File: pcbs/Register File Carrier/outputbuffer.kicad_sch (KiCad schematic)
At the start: 2 parts, among them U4001 74HC245, U4002 74HC245

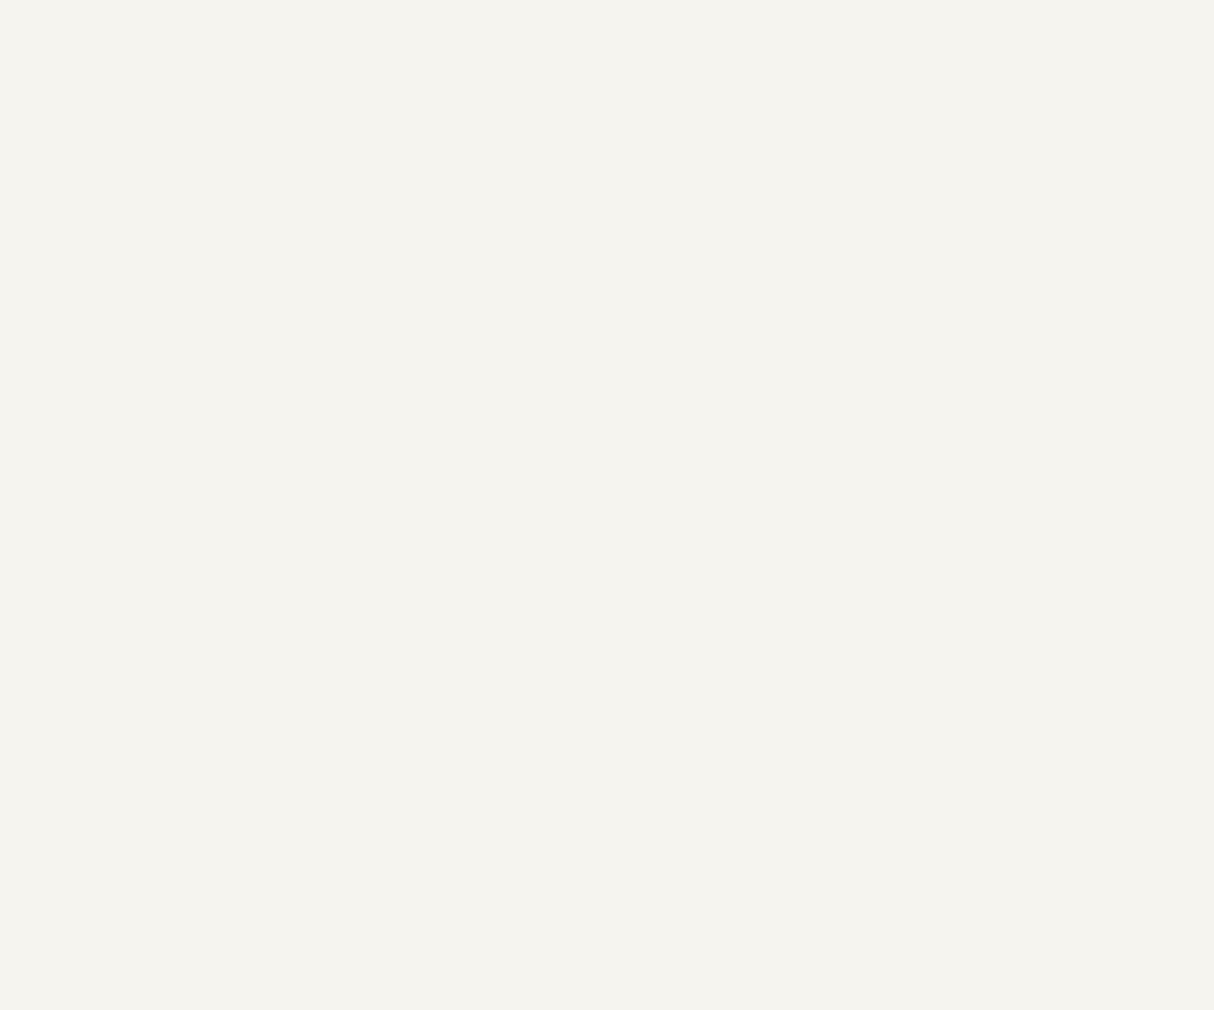
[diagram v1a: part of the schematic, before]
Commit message: Setting up some LEDs
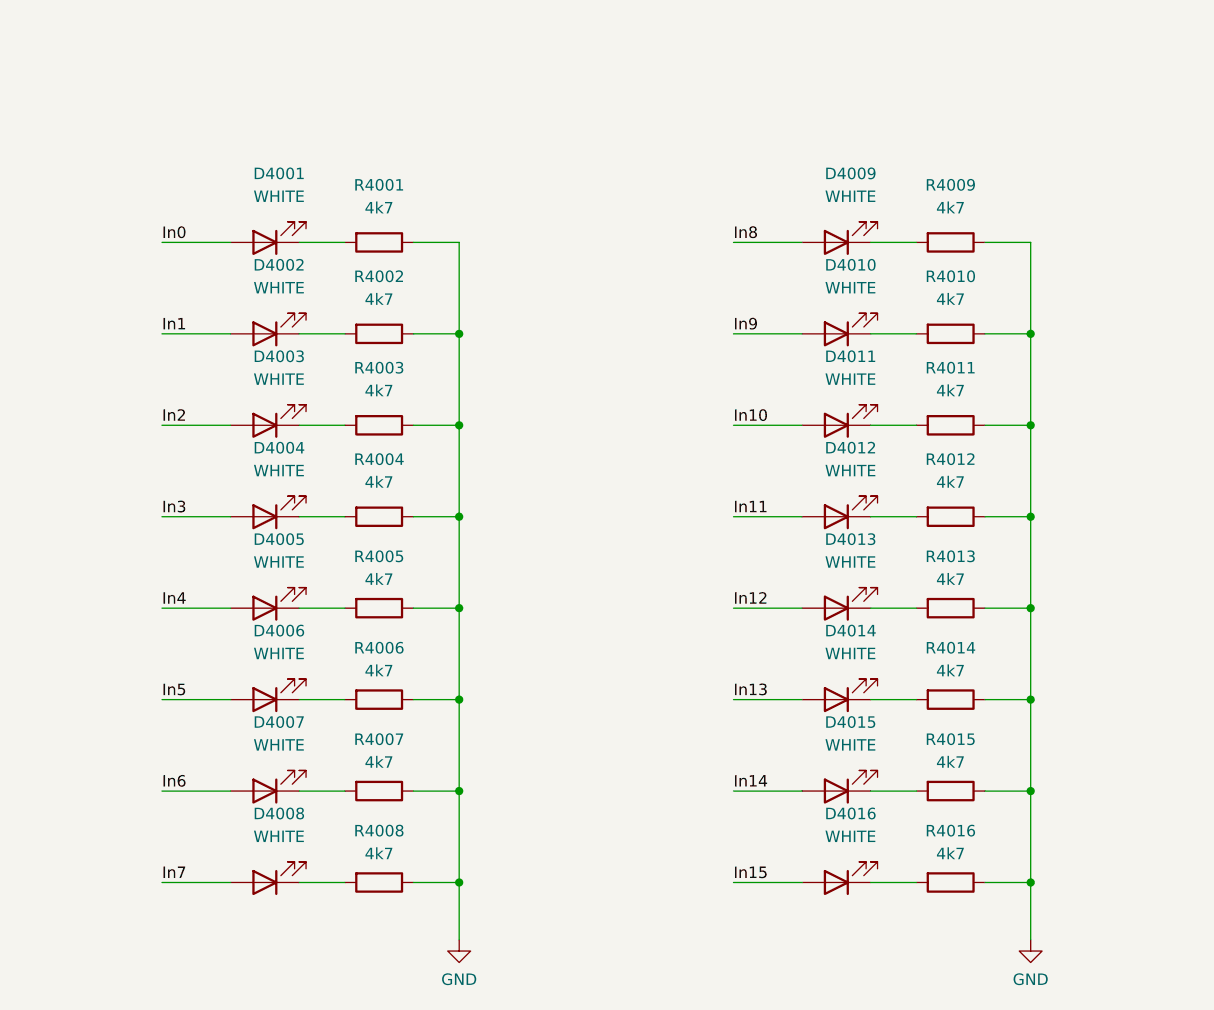
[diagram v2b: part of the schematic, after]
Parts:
- added D4001, D4002, D4003, D4004, D4005, D4006, D4007, D4008, D4009, D4010, D4011, D4012, D4013, D4014, D4015, D4016: WHITE, LED_SMD:LED_0603_1608Metric, symbol Device:LED
- added R4001, R4002, R4003, R4004, R4005, R4006, R4007, R4008, R4009, R4010, R4011, R4012, R4013, R4014, R4015, R4016: 4k7, Resistor_SMD:R_0603_1608Metric, symbol Device:R
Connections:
- net GND: now also R4001.1, R4002.1, R4003.1, R4004.1, R4005.1, R4006.1, R4007.1, R4008.1, R4009.1, R4010.1, R4011.1, R4012.1, R4013.1, R4014.1, R4015.1, R4016.1
- net In0: now also D4001.2 (A)
- net In1: now also D4002.2 (A)
- net In10: now also D4011.2 (A)
- net In11: now also D4012.2 (A)
- net In12: now also D4013.2 (A)
- net In13: now also D4014.2 (A)
- net In14: now also D4015.2 (A)
- net In15: now also D4016.2 (A)
- net In2: now also D4003.2 (A)
- net In3: now also D4004.2 (A)
- net In4: now also D4005.2 (A)
- net In5: now also D4006.2 (A)
- net In6: now also D4007.2 (A)
- net In7: now also D4008.2 (A)
- net In8: now also D4009.2 (A)
- net In9: now also D4010.2 (A)
- new net: D4013.1 (K), R4013.2
- new net: D4012.1 (K), R4012.2
- new net: D4015.1 (K), R4015.2
- new net: D4011.1 (K), R4011.2
- new net: D4008.1 (K), R4008.2
- new net: D4005.1 (K), R4005.2
- new net: D4009.1 (K), R4009.2
- new net: D4006.1 (K), R4006.2
- new net: D4016.1 (K), R4016.2
- new net: D4002.1 (K), R4002.2
- new net: D4004.1 (K), R4004.2
- new net: D4010.1 (K), R4010.2
- new net: D4001.1 (K), R4001.2
- new net: D4007.1 (K), R4007.2
- new net: D4003.1 (K), R4003.2
- new net: D4014.1 (K), R4014.2

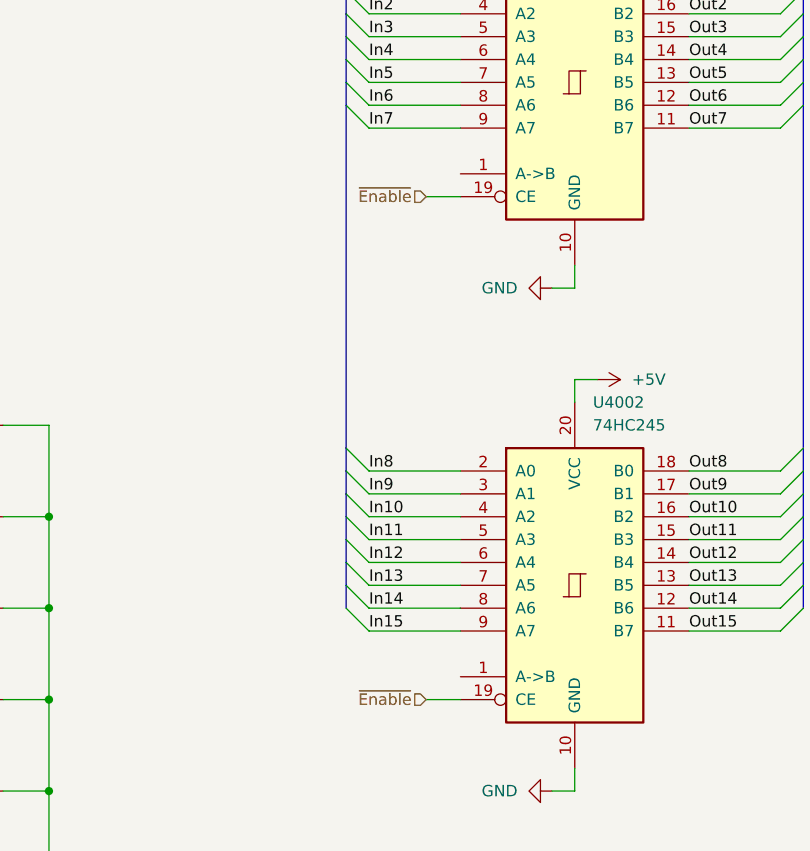
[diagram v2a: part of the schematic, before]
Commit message: More LEDs and routing
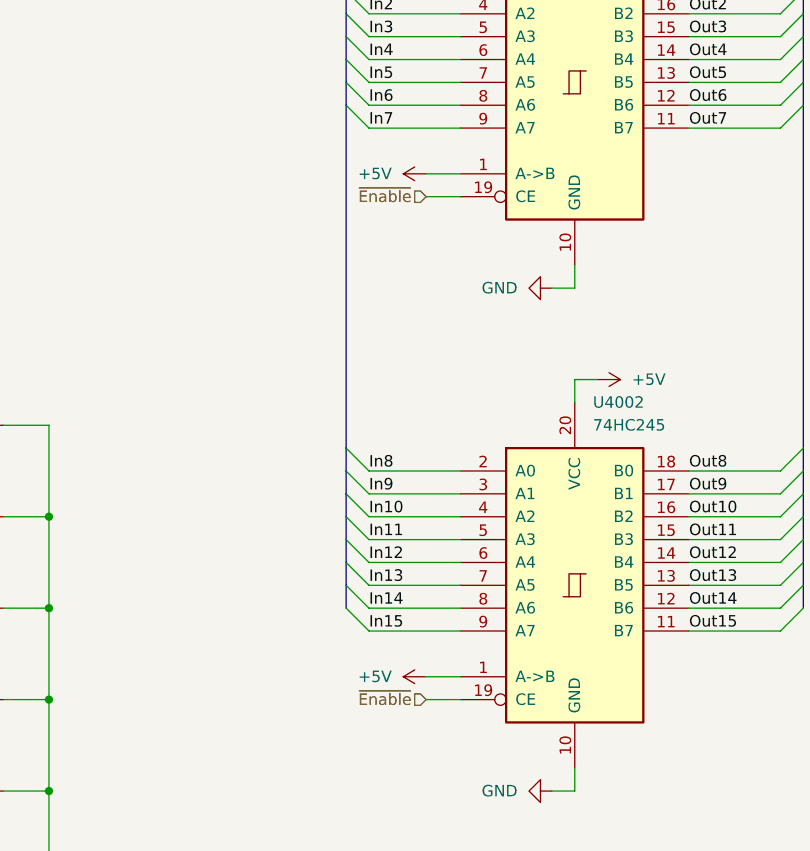
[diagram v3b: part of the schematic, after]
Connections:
- net +5V: now also U4001.1 (A->B), U4002.1 (A->B)
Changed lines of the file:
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@@
 	(wire
 		(pts
+			(xy 199.39 71.12) (xy 203.2 71.12)
+		)
+		(stroke
+			(width 0)
+			(type default)
+		)
+	)
+	(wire
+		(pts
 			(xy 93.98 129.54) (xy 93.98 119.38)
 		)
@@
 	(wire
 		(pts
+			(xy 199.39 127) (xy 203.2 127)
+		)
+		(stroke
+			(width 0)
+			(type default)
+		)
+	)
+	(wire
+		(pts
 			(xy 76.2 149.86) (xy 81.28 149.86)
 		)
@@
 	)
 	(symbol
+		(lib_id "power:+5V")
+		(at 199.39 71.12 90)
+		(unit 1)
+		(exclude_from_sim no)
+		(in_bom yes)
+		(on_board yes)
+		(dnp no)
+		(fields_autoplaced yes)
+		(property "Reference" "#PWR04007"
+			(at 203.2 71.12 0)
+			(effects
+				(font
+					(size 1.27 1.27)
+				)
+				(hide yes)
+			)
+		)
+		(property "Value" "+5V"
+			(at 195.58 71.1199 90)
+			(effects
+				(font
+					(size 1.27 1.27)
+				)
+				(justify left)
+			)
+		)
+		(property "Footprint" ""
+			(at 199.39 71.12 0)
+			(effects
+				(font
+					(size 1.27 1.27)
+				)
+				(hide yes)
+			)
+		)
+		(property "Datasheet" ""
+			(at 199.39 71.12 0)
+			(effects
+				(font
+					(size 1.27 1.27)
+				)
+				(hide yes)
+			)
+		)
+		(property "Description" "Power symbol creates a global label with name \"+5V\""
+			(at 199.39 71.12 0)
+			(effects
+				(font
+					(size 1.27 1.27)
+				)
+				(hide yes)
+			)
+		)
+		(pin "1"
+		)
+		(instances
+			(project ""
+				(path "/65c451e4-a769-4416-8c85-372525d2bb28/0d5f3d4f-36a3-45de-b491-16cfbe0721cc"
+					(reference "#PWR04007")
+					(unit 1)
+				)
+				(path "/65c451e4-a769-4416-8c85-372525d2bb28/17ce0966-f887-496c-87c5-a71274f25321"
+					(reference "#PWR05007")
+					(unit 1)
+				)
+			)
+		)
+	)
+	(symbol
 		(lib_id "Device:LED")
 		(at 72.39 109.22 180)
@@
 					(unit 1)
 				)
+			)
+		)
+	)
+	(symbol
+		(lib_id "power:+5V")
+		(at 199.39 127 90)
+		(unit 1)
+		(exclude_from_sim no)
+		(in_bom yes)
+		(on_board yes)
+		(dnp no)
+		(fields_autoplaced yes)
+		(property "Reference" "#PWR04008"
+			(at 203.2 127 0)
+			(effects
+				(font
+					(size 1.27 1.27)
+				)
+				(hide yes)
+			)
+		)
+		(property "Value" "+5V"
+			(at 195.58 126.9999 90)
+			(effects
+				(font
+					(size 1.27 1.27)
+				)
+				(justify left)
+			)
+		)
+		(property "Footprint" ""
+			(at 199.39 127 0)
+			(effects
+				(font
+					(size 1.27 1.27)
+				)
+				(hide yes)
+			)
+		)
+		(property "Datasheet" ""
+			(at 199.39 127 0)
+			(effects
+				(font
+					(size 1.27 1.27)
+				)
+				(hide yes)
+			)
+		)
+		(property "Description" "Power symbol creates a global label with name \"+5V\""
+			(at 199.39 127 0)
+			(effects
+				(font
+					(size 1.27 1.27)
+				)
+				(hide yes)
+			)
+		)
+		(pin "1"
+		)
+		(instances
+			(project "Register File Carrier"
+				(path "/65c451e4-a769-4416-8c85-372525d2bb28/0d5f3d4f-36a3-45de-b491-16cfbe0721cc"
+					(reference "#PWR04008")
+					(unit 1)
+				)
+				(path "/65c451e4-a769-4416-8c85-372525d2bb28/17ce0966-f887-496c-87c5-a71274f25321"
+					(reference "#PWR05008")
+					(unit 1)
+				)

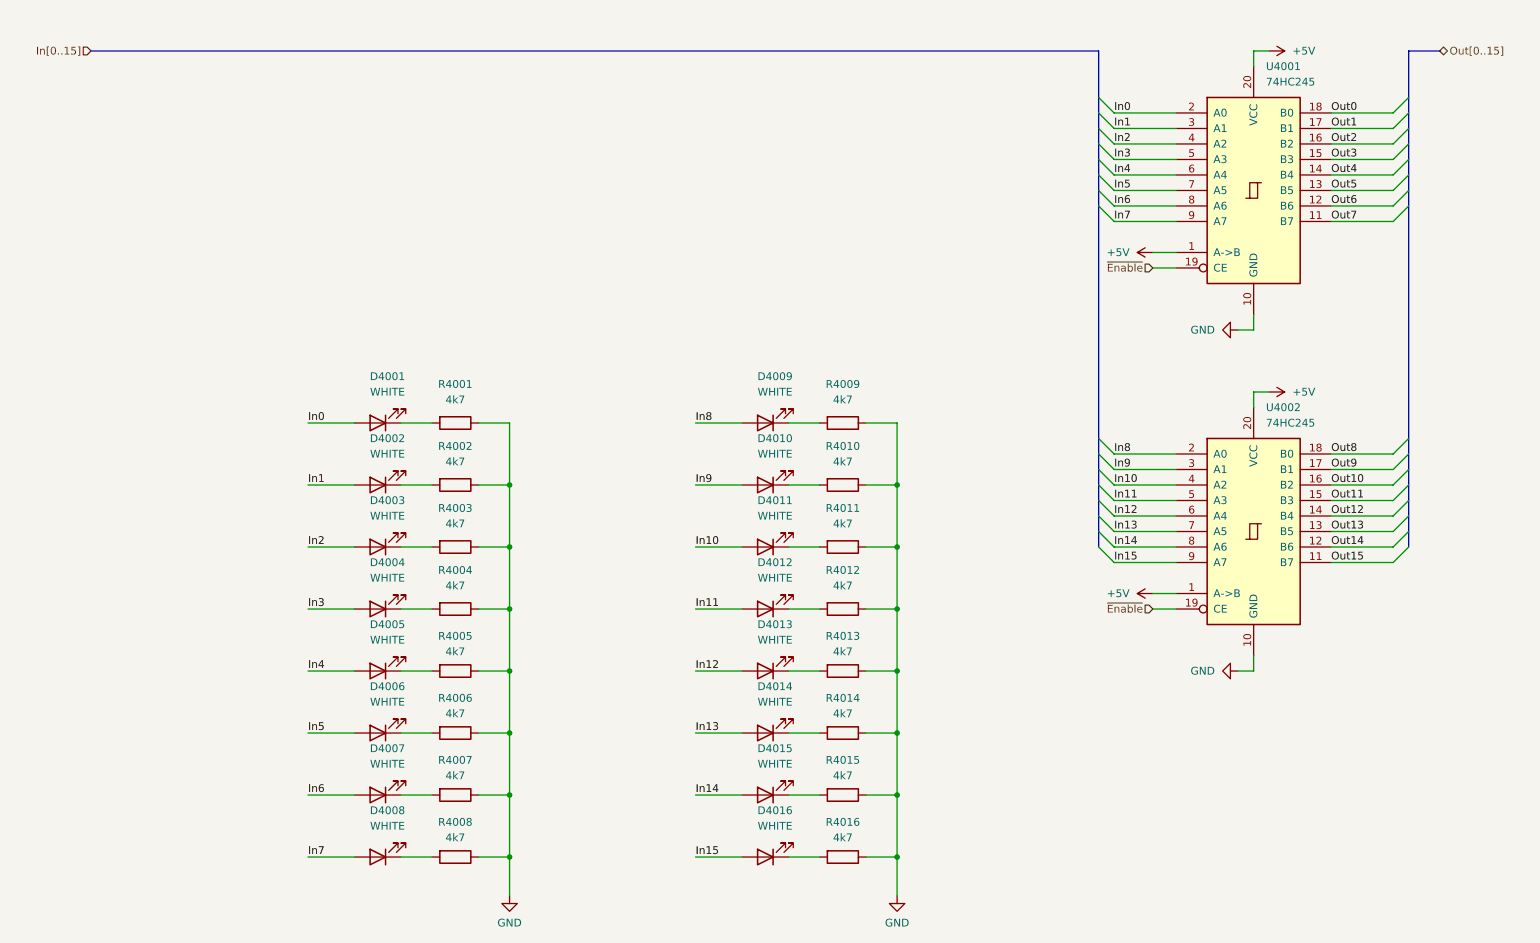
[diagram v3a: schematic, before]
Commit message: Output buffers were a bad idea which were about to cause trouble
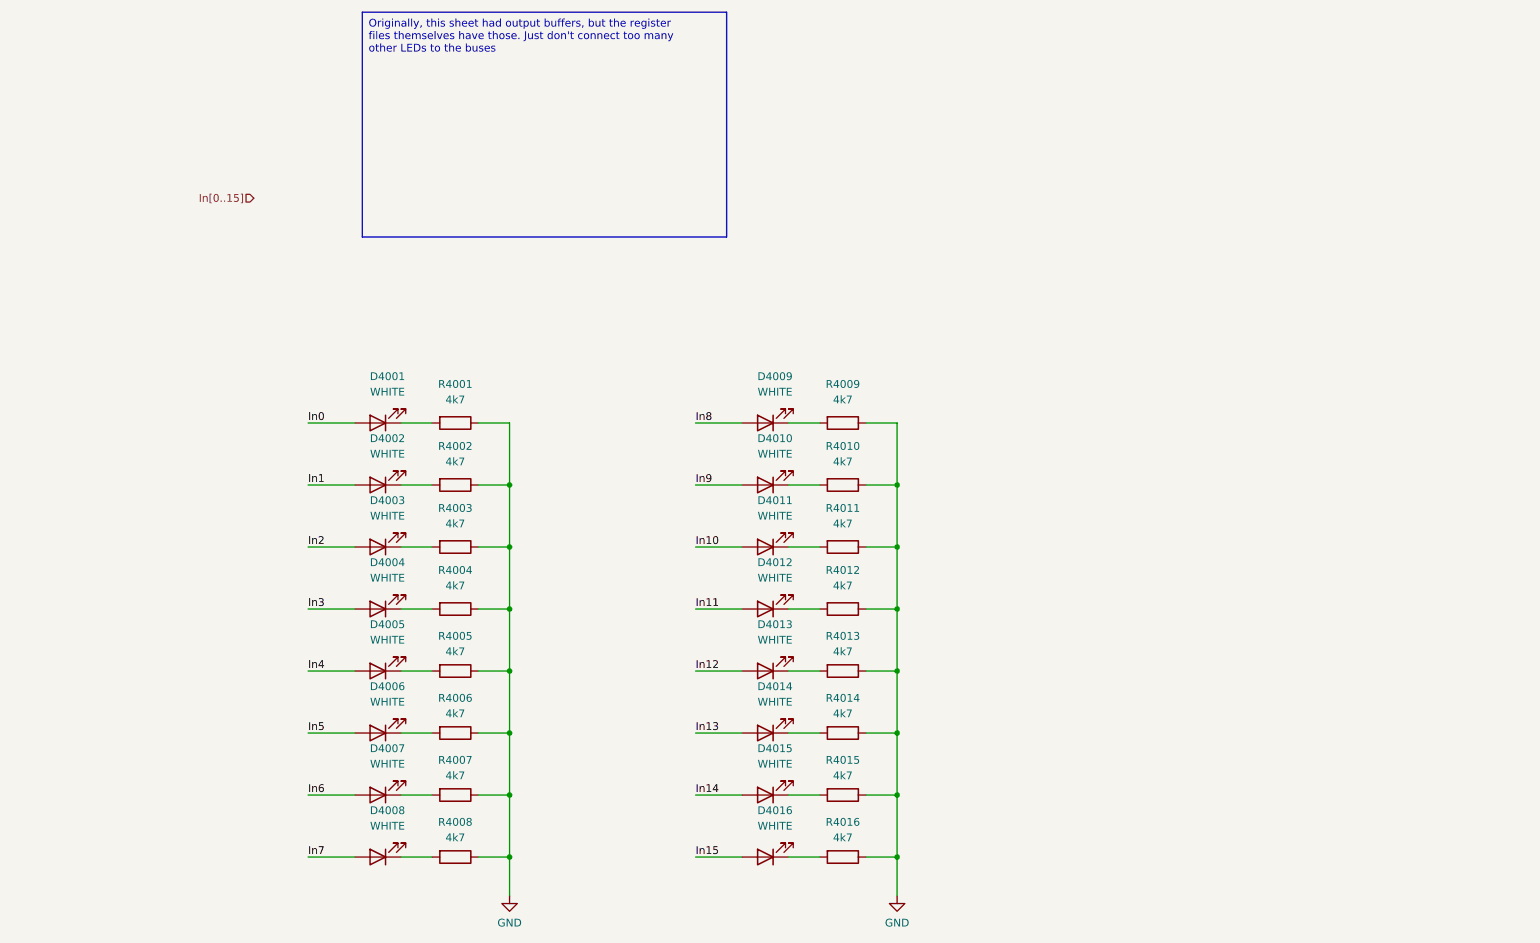
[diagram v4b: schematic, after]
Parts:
- removed U4001, U4002: 74HC245, Package_SO:SOIC-20W_7.5x12.8mm_P1.27mm, symbol 74xx:74HC245
